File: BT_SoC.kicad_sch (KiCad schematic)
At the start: 12 parts, among them J7 Conn_02x08_Odd_Even, J8 Conn_02x08_Odd_Even, U1 BM83SM1-00TB

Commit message: 3D models.
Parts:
- U1: Manufacturer_Part_Number (none) -> BM83SM1-00TB
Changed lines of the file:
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@@
 			)
 		)
-		(property "Datasheet" "~"
+		(property "Datasheet" "Datasheet/PYu_RC_Group_51_RoHS_L_11-1984063.pdf"
 			(at 190.5 67.31 0)
 			(effects
@@
 			)
 		)
-		(property "Datasheet" "~"
+		(property "Datasheet" "Datasheet/PYu_RC_Group_51_RoHS_L_11-1984063.pdf"
 			(at 190.5 64.77 0)
 			(effects
@@
 			)
 		)
-		(property "Datasheet" "~"
+		(property "Datasheet" "Datasheet/General_Purpose_Capacitors-3314795.pdf"
 			(at 33.02 31.75 0)
 			(effects
@@
 			)
 		)
+		(property "Manufacturer_Part_Number" "BM83SM1-00TB"
+			(at 106.68 59.69 0)
+			(effects
+				(font
+					(size 1.27 1.27)
+				)
+				(hide yes)
+			)
+		)
 		(pin "4"
 		)
@@
 			)
 		)
-		(property "Datasheet" "EAST16084BA8"
+		(property "Datasheet" "Datasheet/EAST16084BA8-3433911.pdf"
 			(at 204.47 100.33 0)
 			(effects
@@
 			)
 		)
-		(property "Datasheet" "~"
+		(property "Datasheet" "Datasheet/PYu_RC_Group_51_RoHS_L_11-1984063.pdf"
 			(at 190.5 59.69 0)
 			(effects
@@
 			)
 		)
-		(property "Datasheet" "~"
+		(property "Datasheet" "Datasheet/PYu_RC_Group_51_RoHS_L_11-1984063.pdf"
 			(at 190.5 62.23 0)
 			(effects
@@
 			)
 		)
-		(property "Datasheet" "~"
+		(property "Datasheet" "Datasheet/KGM_X7R-3223212.pdf"
 			(at 40.64 31.75 0)
 			(effects
@@
 			)
 		)
-		(property "Datasheet" "~"
+		(property "Datasheet" "Datasheet/cx5r_KGM-3223198.pdf"
 			(at 24.13 31.75 0)
 			(effects
@@
 			)
 		)
-		(property "Datasheet" "EAST16084BA8"
+		(property "Datasheet" "Datasheet/EAST16084BA8-3433911.pdf"
 			(at 213.36 101.6 0)
 			(effects

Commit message: Place and align PCB components to enclosure DXF. Expand PCB 15mm both sides of USB-C. Move BM83 to right side. Cutout PCB along right side for antenna function.
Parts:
- removed J7, J8: Conn_02x08_Odd_Even, Connector_PinHeader_2.54mm:PinHeader_2x08_P2.54mm_Vertical, symbol Mustang_Library:Conn_02x08_Odd_Even
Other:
- moved on the sheet: C118, C119, C123, LED1, LED2, R67, R68, R69, R70, U1

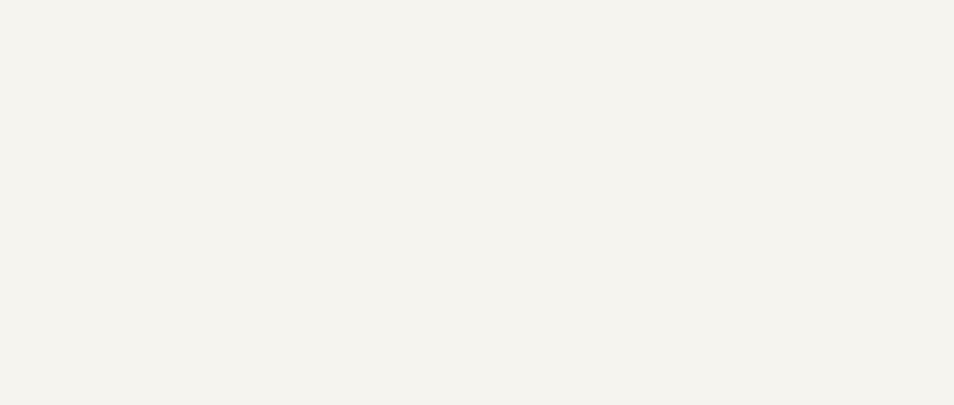
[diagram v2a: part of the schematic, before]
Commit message: Electrical Rules Check fixes in progress.
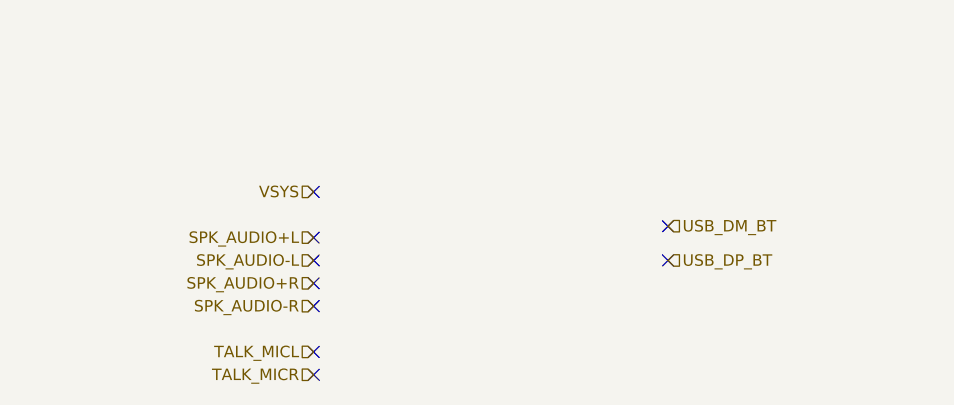
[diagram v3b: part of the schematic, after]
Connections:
- no-connect marks 5 -> 14
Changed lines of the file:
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@@
 	)
 	(no_connect
+		(at 482.6 534.67)
+	)
+	(no_connect
+		(at 443.23 547.37)
+	)
+	(no_connect
+		(at 443.23 544.83)
+	)
+	(no_connect
+		(at 443.23 527.05)
+	)
+	(no_connect
 		(at 396.24 378.46)
 	)
@@
 	)
 	(no_connect
+		(at 443.23 539.75)
+	)
+	(no_connect
+		(at 443.23 537.21)
+	)
+	(no_connect
+		(at 443.23 534.67)
+	)
+	(no_connect
+		(at 482.6 530.86)
+	)
+	(no_connect
 		(at 378.46 397.51)
 	)
@@
 		(at 396.24 381)
 	)
+	(no_connect
+		(at 443.23 532.13)
+	)
 	(wire
 		(pts
@@
 		)
 	)
+	(hierarchical_label "USB_DM_BT"
+		(shape input)
+		(at 482.6 530.86 0)
+		(fields_autoplaced yes)
+		(effects
+			(font
+				(size 1.27 1.27)
+			)
+			(justify left)
+		)
+	)
+	(hierarchical_label "SPK_AUDIO-R"
+		(shape input)
+		(at 443.23 539.75 180)
+		(fields_autoplaced yes)
+		(effects
+			(font
+				(size 1.27 1.27)
+			)
+			(justify right)
+		)
+	)
+	(hierarchical_label "TALK_MICR"
+		(shape input)
+		(at 443.23 547.37 180)
+		(fields_autoplaced yes)
+		(effects
+			(font
+				(size 1.27 1.27)
+			)
+			(justify right)
+		)
+	)
+	(hierarchical_label "TALK_MICL"
+		(shape input)
+		(at 443.23 544.83 180)
+		(fields_autoplaced yes)
+		(effects
+			(font
+				(size 1.27 1.27)
+			)
+			(justify right)
+		)
+	)
+	(hierarchical_label "USB_DP_BT"
+		(shape input)
+		(at 482.6 534.67 0)
+		(fields_autoplaced yes)
+		(effects
+			(font
+				(size 1.27 1.27)
+			)
+			(justify left)
+		)
+	)
+	(hierarchical_label "SPK_AUDIO+L"
+		(shape input)
+		(at 443.23 532.13 180)
+		(fields_autoplaced yes)
+		(effects
+			(font
+				(size 1.27 1.27)
+			)
+			(justify right)
+		)
+	)
+	(hierarchical_label "SPK_AUDIO+R"
+		(shape input)
+		(at 443.23 537.21 180)
+		(fields_autoplaced yes)
+		(effects
+			(font
+				(size 1.27 1.27)
+			)
+			(justify right)
+		)
+	)
+	(hierarchical_label "VSYS"
+		(shape input)
+		(at 443.23 527.05 180)
+		(fields_autoplaced yes)
+		(effects
+			(font
+				(size 1.27 1.27)
+			)
+			(justify right)
+		)
+	)
+	(hierarchical_label "SPK_AUDIO-L"
+		(shape input)
+		(at 443.23 534.67 180)
+		(fields_autoplaced yes)
+		(effects
+			(font
+				(size 1.27 1.27)
+			)
+			(justify right)
+		)
+	)

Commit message: wip
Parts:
- removed LED1, LED2: EAST16084BA8, Mustang_Library:LED_EAST16084BA8_EVE, symbol Mustang_Library:EAST16084BA8
- removed R67, R68, R69, R70: 33R, Mustang_Library:R_0402_1005Metric, symbol Mustang_Library:R_Small_US
- added D9: EAST1616RGBA3, Mustang_Library:LED_EAST1616RGBA3, symbol Mustang_Library:EAST1616RGBA3
- added R20, R21, R22, R23, R24: 24R, symbol Mustang_Library:R_h
- U1: footprint Mustang_Library:Microchip_BM83 -> Mustang_Library:BM83_MCH
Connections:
- net AIL: no longer U1.12 (AIL)
- net AIR: no longer U1.11 (AIR)
- net GND: no longer U1.16 (GND), U1.50 (GND), U1.56 (GND), U1.57 (GND)
- net LEFT_TM_OUT: no longer U1.14 (MICP1)
- net P_EN: no longer U1.26 (PWR(MFB))
- net RIGHT_TM_OUT: no longer U1.10 (MICP2)
- net RST_N: no longer U1.43 (RST_N)
- net SPK-: no longer U1.7 (AOHPM)
- net SPKL+: no longer U1.8 (AOHPL)
- net SPKR+: no longer U1.6 (AOHPR)
- net SYS_PWR: now also D9.3; no longer U1.24 (SYS_PWR)
- net USART1CTS: now also R22.2
- net USART1RTS: now also R23.2
- net USART1Rx: now also R20.2
- net USART1Tx: now also R21.2
- net Wakeup: now also R24.2; no longer U1.49 (P0_0/UART_TX_IND)
- net i2SMCK: no longer U1.3 (SCLK1), U1.5 (MCLK1)
- net i2SMDR1: no longer U1.1 (DR1)
- net i2SMDT1: no longer U1.4 (DT1)
- net i2SMRFS1: no longer U1.2 (RFS1)
- net at U1.48 (P3_7/UART_CTS): now also R23.1
- net at U1.31 (P3_4/UART_RTS): now also R22.1
- net at U1.29 (P8_6/UART_RXD): now also R21.1
- net at U1.30 (P8_5/UART_TXD): now also R20.1
- new net: R24.1, U1.49 (P0_0/UART_TX_IND)
- no-connect marks 14 -> 13

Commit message: wip
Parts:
- removed C118: .1uF, Mustang_Library:C_0402_1005Metric, symbol Mustang_Library:C_Small
- removed C119: 10nF, Mustang_Library:C_0402_1005Metric, symbol Mustang_Library:C_Small
- removed C123: 1uF, Mustang_Library:C_0402_1005Metric, symbol Mustang_Library:C_Small
- added C14, C19: .1uF, Mustang_Library:C_0402_1005Metric, symbol Mustang_Library:C_Small
- added C15, C16: 10nF, Mustang_Library:C_0402_1005Metric, symbol Mustang_Library:C_Small
- added C17, C18: 1uF, Mustang_Library:C_0805_2012Metric_Pad1.18x1.45mm_HandSolder, symbol Mustang_Library:C
- added R25, R26, R27, R28, R29, R30, R31, R32, R33, R34, R35, R36, R37, R38, R39, R40, R41, R42, R47, R48, R54, R55, R56, R60, R61, R62: 24R, symbol Mustang_Library:R_h
- added R43, R44, R46, R49, R50, R51, R52, R53, R57, R58, R59, R63, R64, R65, R66, R67, R68, R69: 0R, symbol Mustang_Library:R_h
- added U5: LP5907MFX-3.3_NOPB, Mustang_Library:SOT95P280X145-5N, symbol LP5907MFX-3.3:LP5907MFX-3.3_NOPB
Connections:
- net AIL: now also R48.1
- net AIR: now also R47.1
- net GND: now also U1.16 (GND), U1.50 (GND), U1.56 (GND), U1.57 (GND), C14.2, C15.2, C16.2, C17.2, C18.2, C19.2, U5.2 (GND)
- net P0_2: now also R28.2; no longer U1.33 (P0_2)
- net P0_3: now also R29.2; no longer U1.38 (P0_3)
- net P0_5: now also R30.2; no longer U1.40 (P0_5)
- net P0_6: now also R31.2; no longer U1.35 (P0_6)
- net P0_7: now also R32.2; no longer U1.45 (P0_7)
- net P2_3: now also R34.2; no longer U1.42 (P2_3)
- net P2_6: now also R35.2; no longer U1.21 (P2_6)
- net P2_7: now also R36.2; no longer U1.39 (P2_7)
- net P3_2: now also R37.2; no longer U1.20 (P3_2)
- net RST_N: now also R62.1
- net SYS_PWR: now also R59.1
- net VSYS: now also C17.1, U5.1 (IN)
- net at D9.2: now also R64.1
- net at D9.4: now also R63.1
- net at U1.1 (DR1): now also R38.2
- net at U1.10 (MICP2): now also R50.2
- net at U1.11 (AIR): now also R47.2
- net at U1.12 (AIL): now also R48.2
- net at U1.13 (MICN1): now also R51.2
- net at U1.14 (MICP1): now also R52.2
- net at U1.15 (MICBIAS): now also R53.2
- net at U1.17 (DMIC_CLK): now also R54.2
- net at U1.18 (DMIC1_R): now also R55.2
- net at U1.19 (DMIC1_L): now also R56.2
- net at U1.2 (RFS1): now also R39.2
- net at U1.22 (ADAP_IN): now also C19.1, R57.2
- net at U1.23 (BAT_IN): now also C14.1, R58.2
- net at U1.24 (SYS_PWR): now also R59.2
- net at U1.25 (VDD_IO): now also R60.2
- net at U1.26 (PWR(MFB)): now also R61.2
- net at U1.27 (SKI_AMB_DET): now also C15.1, R65.2
- net at U1.28 (SK2_KEY_AD): now also C16.1, R66.2
- net at U1.3 (SCLK1): now also R40.2
- net at U1.32 (LED1): now also R63.2
- net at U1.34 (LED2): now also R64.2
- net at U1.4 (DT1): now also R41.2
- net at U1.43 (RST_N): now also R62.2
- net at U1.5 (MCLK1): now also R42.2
- net at U1.6 (AOHPR): now also R43.2
- net at U1.7 (AOHPM): now also R44.2, R67.2
- net at U1.8 (AOHPL): now also R46.2
- net at U1.9 (MICN2): now also R49.2
- net BTDM renamed USB_DM
- net BTDP renamed USB_DP
- net P0_0: no longer names the net of U1.44 (P0_1)
- net P0_0: now also R27.1
- net PWM1: no longer names the net of U1.41 (P1_6/PWM1)
- net PWM1: now also R33.1
- net TCK_CPU: no longer names the net of U1.47 (P1_3/TCK_CPU/SDA)
- net TCK_CPU: now also R25.1
- net TDI_CPU: no longer names the net of U1.46 (P1_2/TDI_CPU/SCL)
- net TDI_CPU: now also R26.1
- net USART1CTS renamed UART_RTS
- net USART1RTS renamed UART_CTS
- net USART1Rx renamed UART_TXD
- net USART1Tx renamed UART_RXD
- net Wakeup renamed UART_TX_IND
- new net: R37.1, U1.20 (P3_2)
- new net: C18.1, R58.1, R68.2, R69.2, U5.5 (OUT)
- new net: R30.1, U1.40 (P0_5)
- new net: R31.1, U1.35 (P0_6)
- new net: R32.1, U1.45 (P0_7)
- new net: R36.1, U1.39 (P2_7)
- new net: R29.1, U1.38 (P0_3)
- new net: R28.1, U1.33 (P0_2)
- new net: R35.1, U1.21 (P2_6)
- new net: R34.1, U1.42 (P2_3)
- new net +3V3: R69.1
- new net DMIC_CLK: R54.1
- new net DMIC_L: R56.1
- new net DMIC_R: R55.1
- new net HPL+: R46.1
- new net HPL-: R67.1
- new net HPR+: R43.1
- new net HPR-: R44.1
- new net I2S_DR: R38.1
- new net I2S_DT: R41.1
- new net I2S_MCLK: R42.1
- new net I2S_RFS: R39.1
- new net I2S_SCLK: R40.1
- new net LDO_EN: U5.3 (EN)
- new net MIC1+: R52.1
- new net MIC1-: R51.1
- new net MIC2+: R50.1
- new net MICBIAS: R53.1
- new net MIN2-: R49.1
- new net P0_1: R27.2
- new net PWM: R33.2
- new net PWR_MFB: R61.1
- new net SCL_TDI: R26.2
- new net SDA_TCK: R25.2
- new net TEMP_AUX: R66.1
- new net TEMP_BATT: R65.1
- new net VBATT: R68.1
- new net VUSB: R57.1
- no-connect marks 13 -> 1
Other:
- note removed: "GND?"
- moved on the sheet: D9, R20, R21, R22, R23, R24

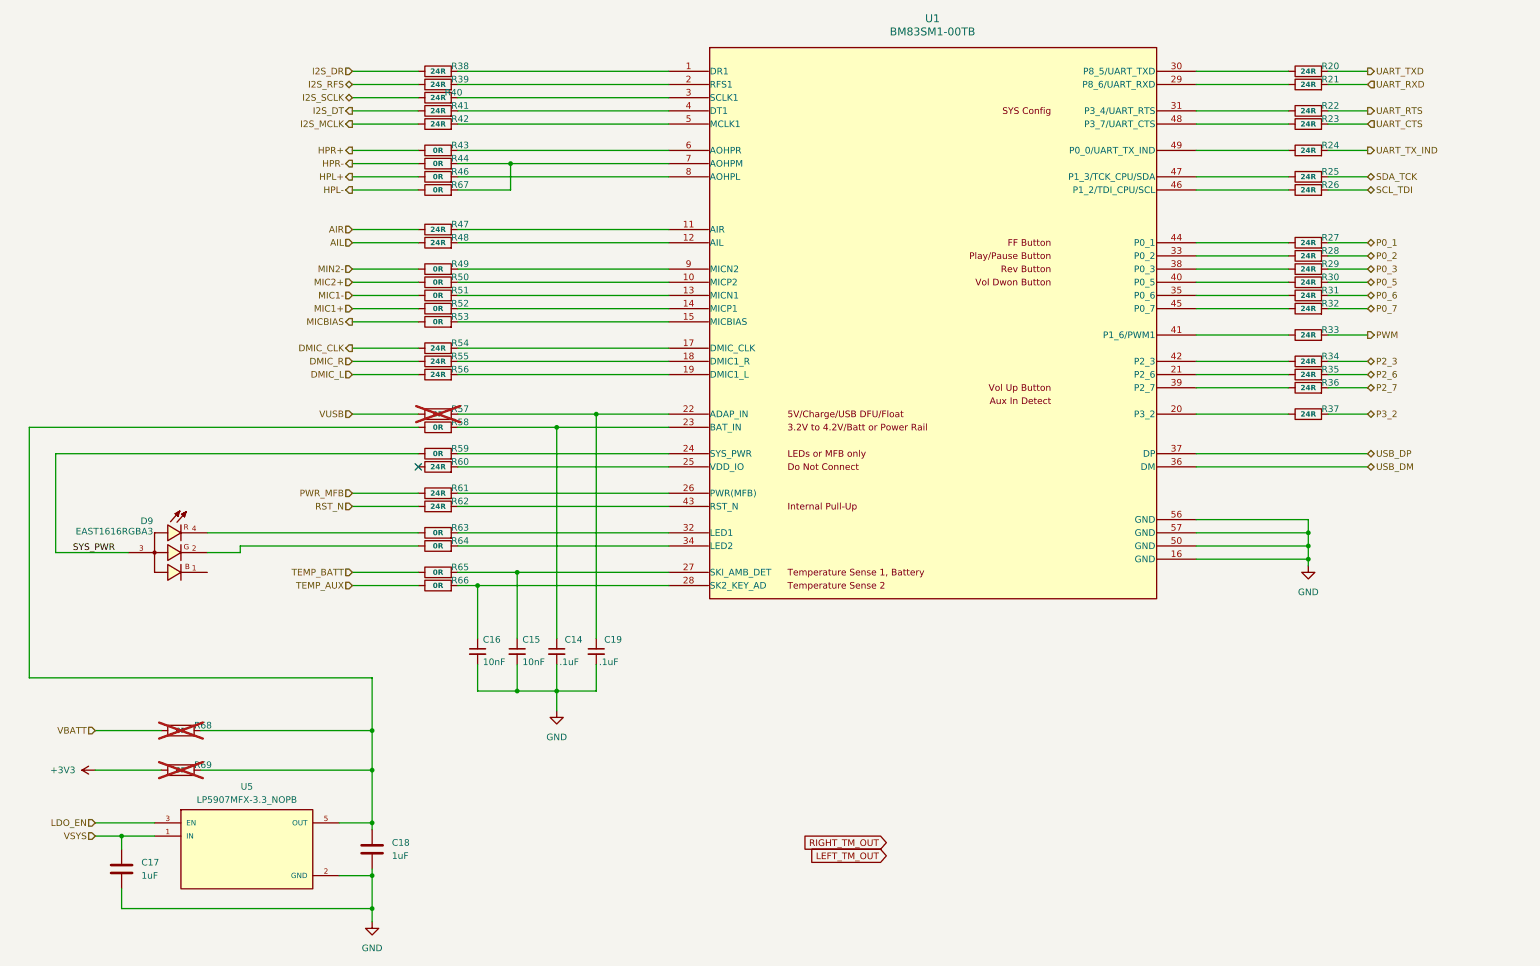
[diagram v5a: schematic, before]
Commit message: Use all YAGEO 0603 resistors.
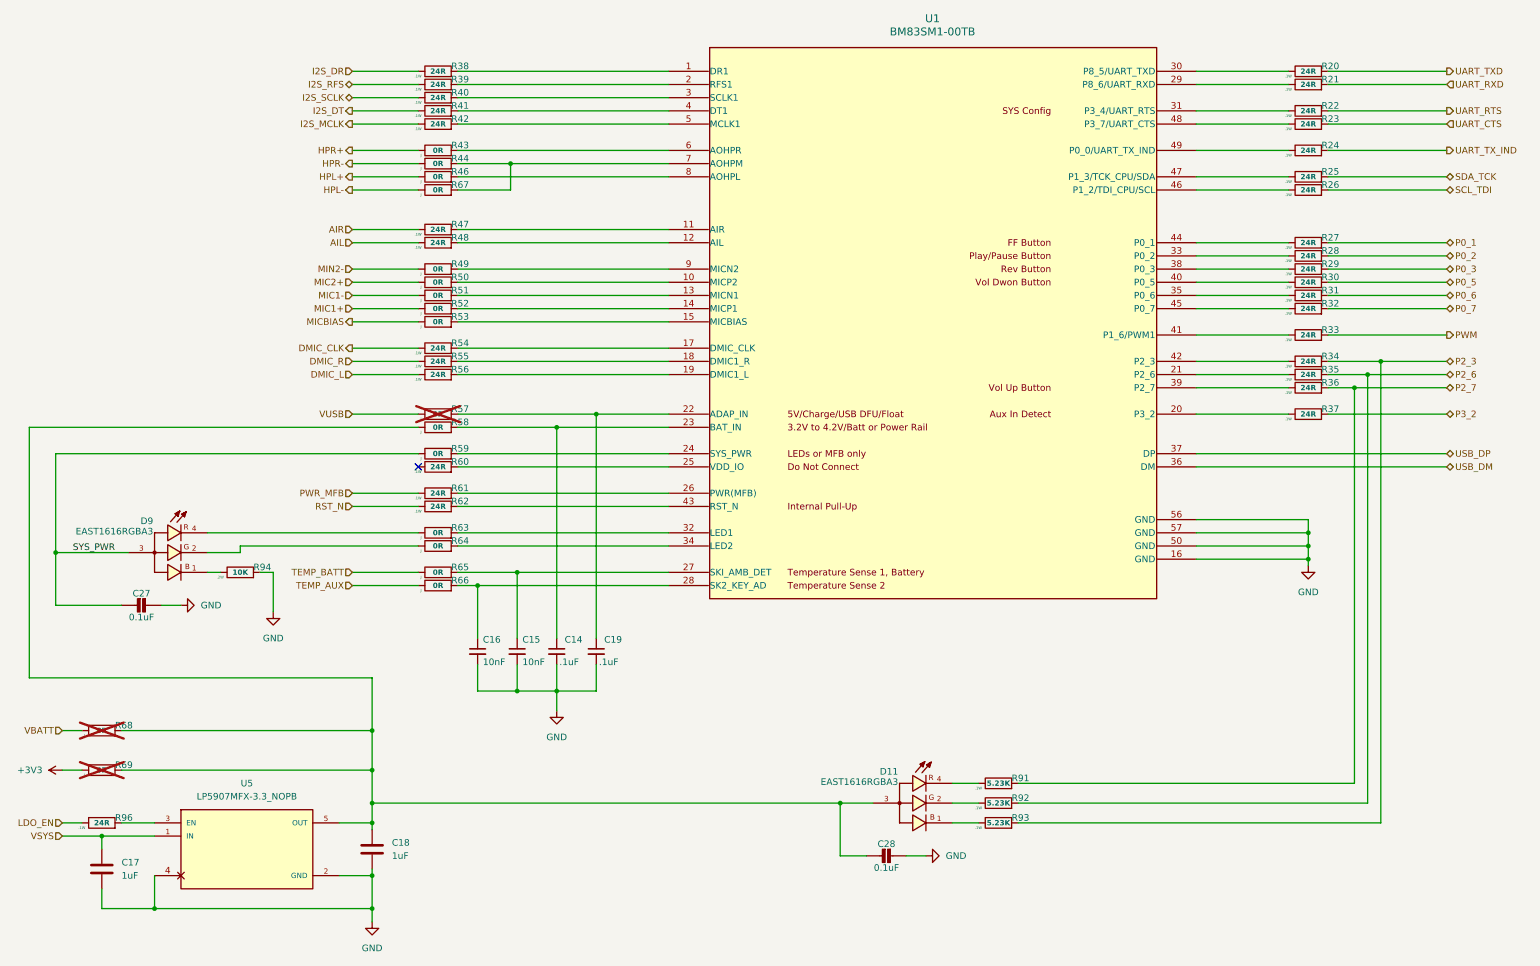
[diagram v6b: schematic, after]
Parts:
- added C27, C28: 0.1uF, Mustang_Library:C_0805_2012Metric_Pad1.18x1.45mm_HandSolder, symbol Mustang_Library:CAP_CERAMIC0805-NOOUTLINE
- added D11: EAST1616RGBA3, Mustang_Library:LED_EAST1616RGBA3, symbol Mustang_Library:EAST1616RGBA3
- added R91, R92, R93: 5.23K, Mustang_Library:R_0603_1608Metric, symbol Mustang_Library:R_0603_5.23K
- added R94: 10K, Mustang_Library:R_0603_1608Metric, symbol Mustang_Library:R_0603_10K
- added R96: 24R, Mustang_Library:R_0603_1608Metric, symbol Mustang_Library:R_0603_24R
- C14, C15, C16, C19: footprint Mustang_Library:C_0402_1005Metric -> Mustang_Library:C_0805_2012Metric_Pad1.18x1.45mm_HandSolder
- R20, R21, R22, R23, R24, R25, R26, R27, R28, R29, R30, R31, R32, R33, R34, R35, R36, R37, R38, R39, R40, R41, R42, R47, R48, R54, R55, R56, R60, R61, R62: footprint (none) -> Mustang_Library:R_0603_1608Metric; symbol Mustang_Library:R_h -> Mustang_Library:R_0603_24R; MPN (none) -> AC0603JR-0724RL; Manufacturer (none) -> Yageo; Power (none) -> .1W
- R43, R44, R46, R49, R50, R51, R52, R53, R57, R58, R59, R63, R64, R65, R66, R67, R68, R69: footprint (none) -> Mustang_Library:R_0603_1608Metric; symbol Mustang_Library:R_h -> Mustang_Library:R_0603_0R; MPN (none) -> AC0603JR-070RL; Manufacturer (none) -> Yageo; Power (none) -> J
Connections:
- net GND: now also U5.4, C27.2, C28.2, R94.2
- net LDO_EN: now also R96.1; no longer U5.3 (EN)
- net P2_3: now also R93.2
- net P2_6: now also R92.2
- net P2_7: now also R91.2
- net SYS_PWR: now also C27.1
- net at D9.1: now also R94.1
- net at C18.1, R58.1, R68.2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: now also C28.1, D11.3
- new net: R96.2, U5.3 (EN)
- new net: D11.2, R92.1
- new net: D11.1, R93.1
- new net: D11.4, R91.1
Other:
- moved on the sheet: C17, R68, R69
